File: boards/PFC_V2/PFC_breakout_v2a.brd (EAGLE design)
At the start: 72.4 x 58.4 mm, 33 parts, among them CN1 1X4-BIG

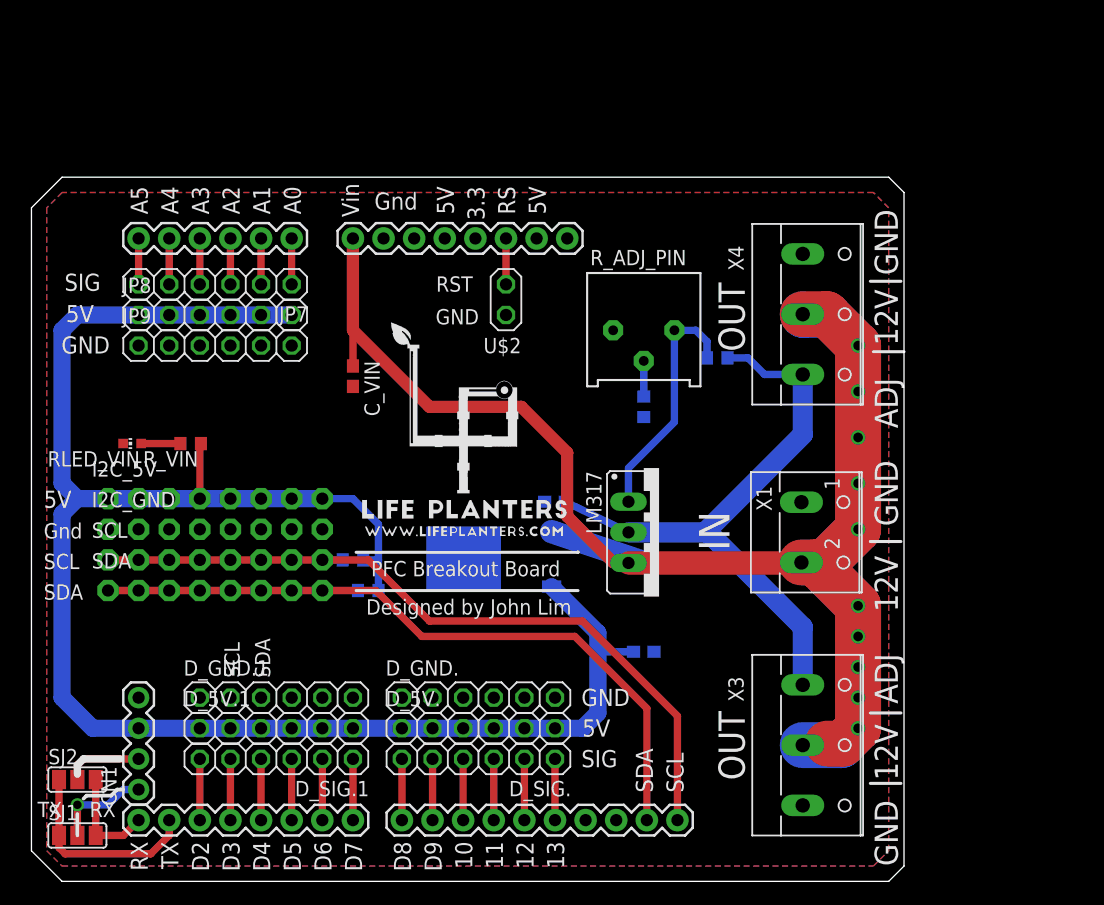
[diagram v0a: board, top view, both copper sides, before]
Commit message: completed ui of touch screen. No integration yet
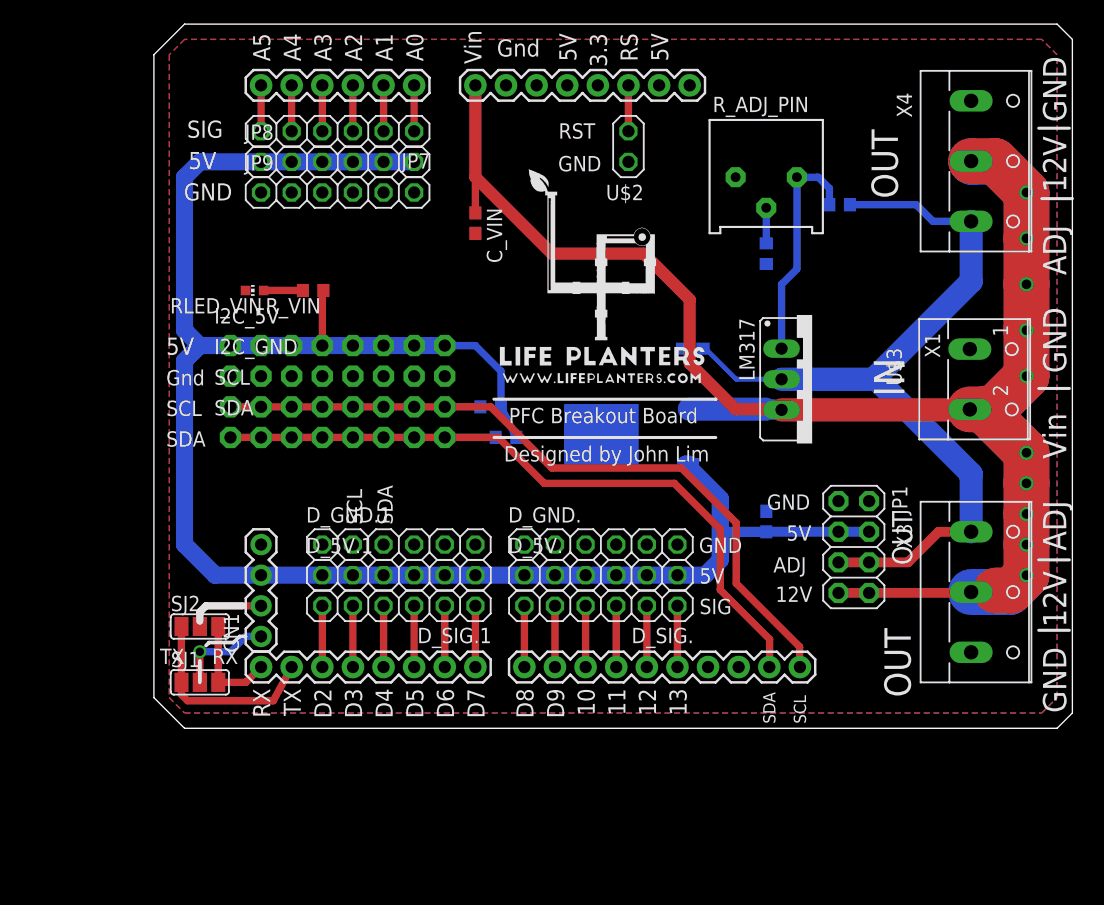
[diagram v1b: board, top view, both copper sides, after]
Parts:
- added JP1: (no value), adafruit:2X04
- added U$3: FW1S, heatsink:FW1S-DOCU
- moved X1 18.9 mm to (84.2, 48.0)
- moved X3 18.9 mm to (84.3, 30.4)
- moved X4 18.9 mm to (84.3, 66.1)
- moved LM317 18.0 mm to (69.8, 48.0)
- moved C_ADJ_PIN 17.1 mm to (59.9, 50.5)
- moved R_VIN1 17.1 mm to (44.5, 43.2)
- moved R_VIN2 17.1 mm to (43.2, 45.7)
- moved U$1 16.3 mm to (87.6, 74.9)
- moved D_5V.1 16.3 mm to (35.6, 31.8)
- moved D_GND.1 16.3 mm to (35.6, 34.3)
- moved D_SIG.1 16.3 mm to (35.6, 29.2)
- moved R2_VREG_PIN 16.3 mm to (66.0, 58.4)
- moved U$2 16.3 mm to (53.3, 67.3)
- moved CN1 16.3 mm to (24.1, 26.7)
- moved C_VIN 16.3 mm to (41.9, 61.0)
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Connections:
- net 5V: now also JP1.3, JP1.4
- net GND: now also JP1.1, JP1.2
- net VIN: now also JP1.7, JP1.8
- net V_ADJ: now also JP1.5, JP1.6
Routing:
- net V_ADJ: track 51.6 -> 70.5 mm
- net VIN: track 161.5 -> 172.2 mm
- net 5V: track 149.5 -> 159.2 mm
- net N$23: track 20.3 -> 19.2 mm
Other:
- board size 72.4 x 58.4 mm -> 76.2 x 58.4 mm

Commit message: boards and src
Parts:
- removed 5VREG: 7805DT, adafruit:TO252
- removed C_5V: 0.1uF, dp_devices:C603
- removed C_ADJ_PIN, C_VIN: 1uF, dp_devices:C603
- removed LM317: (no value), v-reg:317TS
- removed R1_VREG_PIN: 1.86k, resistor:R0603
- removed R2_VREG_PIN: 3k, resistor:R0603
- removed R_ADJ_PIN: 10K, bourns:3386P
- removed X1: (no value), con-wago-500:W237-102
- removed X3, X4: (no value), con-wago-500:W237-103
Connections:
- removed net N$23: LM317.1, R1_VREG_PIN.1, R_ADJ_PIN.3
- removed net N$24: R2_VREG_PIN.2, R_ADJ_PIN.2
- net 5V: no longer 5VREG.2, C_5V.1
- net GND: no longer 5VREG.3, C_5V.2, C_ADJ_PIN.2, C_VIN.2, R2_VREG_PIN.1, X1.1, X3.3, X4.1
- net VIN: no longer 5VREG.1, C_VIN.1, LM317.3, X1.2, X3.2, X4.2
- net V_ADJ: no longer C_ADJ_PIN.1, LM317.2, R1_VREG_PIN.2, X3.1, X4.3
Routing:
- net VIN: track 172.2 -> 55.0 mm, vias 10 -> 0
- net V_ADJ: track 70.5 -> 9.35 mm
- net N$23: track 19.2 -> 0.00 mm
- net 5V: track 159.2 -> 155.3 mm
- net N$24: track 2.96 -> 0.00 mm
